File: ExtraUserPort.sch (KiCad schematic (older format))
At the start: 32 parts, among them CN1 EXPANSION_PORT, CN2 ALMOST_USERPORT, CN3 DB9_MALE, J1 ATTENTION_IN, U1 GAL20V8, U2 MOS_6529, U3 MOS_6551_ACIA, U4 74LS652, U5 MAX238, Y1 1.8432M

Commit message: WIP
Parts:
- added RN1: 8.2k, Resistor_THT:R_Array_SIP9, symbol Device:R_Network08
- D1, D2, D3, D4, D5, D6, D7, D8: renamed from D?; value D -> 1n4148; footprint (none) -> Diode_THT:D_DO-35_SOD27_P2.54mm_Vertical_KathodeUp
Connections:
- net +5V: now also RN1.1 (common)
- net p0: now also D1.2 (A), U4.4 (A1); no longer CN2.B (D0), D1.1 (K)
- net p1: now also D2.2 (A), U4.5 (A2); no longer CN2.K (D1), D2.1 (K)
- net p2: now also D3.2 (A), U4.6 (A3); no longer CN2.4 (D2), D3.1 (K)
- net p3: now also D4.2 (A), U4.7 (A4); no longer CN2.5 (D3), D4.1 (K)
- net p4: now also D5.2 (A), U4.8 (A5); no longer CN2.6 (D4), D5.1 (K)
- net p5: now also D6.2 (A), U4.9 (A6); no longer CN2.7 (D5), D6.1 (K)
- net p6: now also D7.2 (A), U4.10 (A7); no longer CN2.J (D6), D7.1 (K)
- net p7: now also D8.2 (A), U4.11 (A8); no longer CN2.F (D7), D8.1 (K)
- new net pc0: CN2.B (D0), D1.1 (K), RN1.2 (R1)
- new net pc1: CN2.K (D1), D2.1 (K), RN1.3 (R2)
- new net pc2: CN2.4 (D2), D3.1 (K), RN1.4 (R3)
- new net pc3: CN2.5 (D3), D4.1 (K), RN1.5 (R4)
- new net pc4: CN2.6 (D4), D5.1 (K), RN1.6 (R5)
- new net pc5: CN2.7 (D5), D6.1 (K), RN1.7 (R6)
- new net pc6: CN2.J (D6), D7.1 (K), RN1.8 (R7)
- new net pc7: CN2.F (D7), D8.1 (K), RN1.9 (R8)
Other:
- note added: "JP1 CONFIGURES MOS 6529/6551 ADDRESSES:\n1-2 = C16 CONFIGURATION: 6529 = $FD1X, 6551 = $FD0X\n (SAME AS PLUS/4 BUILT-IN PORTS)\n2-3 = PLUS/4 CONFIGURATION: 6529 = $FD7X, 6551 = $FD6X\n (FOR ADDITIONAL PORTS)"
- note added: "MOS 6529 REPLACEMENT CIRCUIT\nBY DANIEL MANTIONE"
- note added: "THESE COMPONENTS ARE NEEDED TO MAKE THE 74x652 OUTPUTS\nBEHAVE IN AN OPEN-COLLECTOR FASHION, AS THE ORIGINAL MOS\n6529 OUTPUTS DO.\n\nTHEY MUST BE PLACED THIS WAY (I.E. AFTER THE OUTPUTS EVEN IF\nAN ORIGINAL 6529 IS USED) FOR ROUTING REASONS, THEREFORE IF\n74x654 OR ORIGINAL MOS 6529 IS USED: \n- REPLACE D1-8 WITH 0-OHM RESISTORS \n- DO NOT MOUNT RN1"
- note removed: "$FD60-FD63\n(CONFIGURABLE WITH JP1)"
- note removed: "$FD70"
- note removed: "THESE ADDRESSES ARE THE SAME\nAS SOLDER'S "SPOILER" FOR THE\nSIMILAR PROJECT HE WAS WORKING\nON AND APPARENTLY NEVER COMPLETED"
- moved on the sheet: C1, C3, C5, C6, C7, C8, C9, CN2, CN3, D1, D2, D3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

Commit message: WIP
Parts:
- D1, D2, D3, D4, D5, D6, D7, D8: value 1n4148 -> BAT43
- R1, R2, R3: footprint Resistor_THT:R_Axial_DIN0207_L6.3mm_D2.5mm_P10.16mm_Horizontal -> Resistor_THT:R_Axial_DIN0207_L6.3mm_D2.5mm_P2.54mm_Vertical
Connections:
- net p0: now also D1.1 (K); no longer D1.2 (A)
- net p1: now also D2.1 (K); no longer D2.2 (A)
- net p2: now also D3.1 (K); no longer D3.2 (A)
- net p3: now also D4.1 (K); no longer D4.2 (A)
- net p4: now also D5.1 (K); no longer D5.2 (A)
- net p5: now also D6.1 (K); no longer D6.2 (A)
- net p6: now also D7.1 (K); no longer D7.2 (A)
- net p7: now also D8.1 (K); no longer D8.2 (A)
- net pc0: now also D1.2 (A); no longer D1.1 (K)
- net pc1: now also D2.2 (A); no longer D2.1 (K)
- net pc2: now also D3.2 (A); no longer D3.1 (K)
- net pc3: now also D4.2 (A); no longer D4.1 (K)
- net pc4: now also D5.2 (A); no longer D5.1 (K)
- net pc5: now also D6.2 (A); no longer D6.1 (K)
- net pc6: now also D7.2 (A); no longer D7.1 (K)
- net pc7: now also D8.2 (A); no longer D8.1 (K)
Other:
- note added: "THESE COMPONENTS ARE NEEDED TO MAKE THE 74x652 OUTPUTS\nBEHAVE IN AN OPEN-COLLECTOR FASHION, AS THE ORIGINAL MOS\n6529 OUTPUTS DO.\n\nTHEY MUST BE PLACED THIS WAY (I.E. AFTER THE OUTPUTS EVEN IF\nAN ORIGINAL 6529 IS USED) FOR ROUTING REASONS, THEREFORE IF\n74x654 OR ORIGINAL MOS 6529 IS USED, REPLACE D1-8 WITH\n0-OHM RESISTORS.\n\nIF ORIGINAL MOS 6529 IS USED, DO NOT MOUNT RN1 EITHER."
- note removed: "THESE COMPONENTS ARE NEEDED TO MAKE THE 74x652 OUTPUTS\nBEHAVE IN AN OPEN-COLLECTOR FASHION, AS THE ORIGINAL MOS\n6529 OUTPUTS DO.\n\nTHEY MUST BE PLACED THIS WAY (I.E. AFTER THE OUTPUTS EVEN IF\nAN ORIGINAL 6529 IS USED) FOR ROUTING REASONS, THEREFORE IF\n74x654 OR ORIGINAL MOS 6529 IS USED: \n- REPLACE D1-8 WITH 0-OHM RESISTORS \n- DO NOT MOUNT RN1"
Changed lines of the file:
@@
 F 0 "R2" H 6765 7251 50  0000 L CNN
 F 1 "10k" H 6765 7160 50  0000 L CNN
-F 2 "Resistor_THT:R_Axial_DIN0207_L6.3mm_D2.5mm_P10.16mm_Horizontal" V 6625 7205 50  0001 C CNN
+F 2 "Resistor_THT:R_Axial_DIN0207_L6.3mm_D2.5mm_P2.54mm_Vertical" V 6625 7205 50  0001 C CNN
 F 3 "~" H 6695 7205 50  0001 C CNN
 	1    6695 7205
@@
 F 0 "R1" H 6485 7251 50  0000 L CNN
 F 1 "10k" H 6485 7160 50  0000 L CNN
-F 2 "Resistor_THT:R_Axial_DIN0207_L6.3mm_D2.5mm_P10.16mm_Horizontal" V 6345 7205 50  0001 C CNN
+F 2 "Resistor_THT:R_Axial_DIN0207_L6.3mm_D2.5mm_P2.54mm_Vertical" V 6345 7205 50  0001 C CNN
 F 3 "~" H 6415 7205 50  0001 C CNN
 	1    6415 7205
@@
 F 0 "R3" H 2105 6681 50  0000 R CNN
 F 1 "10k" H 2105 6590 50  0000 R CNN
-F 2 "Resistor_THT:R_Axial_DIN0207_L6.3mm_D2.5mm_P10.16mm_Horizontal" V 2105 6635 50  0001 C CNN
+F 2 "Resistor_THT:R_Axial_DIN0207_L6.3mm_D2.5mm_P2.54mm_Vertical" V 2105 6635 50  0001 C CNN
 F 3 "~" H 2175 6635 50  0001 C CNN
 	1    2175 6635
@@
 P 11140 4640
 F 0 "D2" H 11250 4680 50  0000 C CNN
-F 1 "1n4148" H 11140 4766 50  0001 C CNN
+F 1 "BAT43" H 11140 4766 50  0001 C CNN
 F 2 "Diode_THT:D_DO-35_SOD27_P2.54mm_Vertical_KathodeUp" H 11140 4640 50  0001 C CNN
 F 3 "~" H 11140 4640 50  0001 C CNN
 	1    11140 4640
-	-1   0    0    -1
+	1    0    0    -1
 $EndComp
 Wire Wire Line
@@
 P 11445 4740
 F 0 "D3" H 11560 4780 50  0000 C CNN
-F 1 "1n4148" H 11445 4866 50  0001 C CNN
+F 1 "BAT43" H 11445 4866 50  0001 C CNN
 F 2 "Diode_THT:D_DO-35_SOD27_P2.54mm_Vertical_KathodeUp" H 11445 4740 50  0001 C CNN
 F 3 "~" H 11445 4740 50  0001 C CNN
 	1    11445 4740
-	-1   0    0    -1
+	1    0    0    -1
 $EndComp
 Wire Wire Line
@@
 P 11140 4840
 F 0 "D4" H 11250 4885 50  0000 C CNN
-F 1 "1n4148" H 11140 4966 50  0001 C CNN
+F 1 "BAT43" H 11140 4966 50  0001 C CNN
 F 2 "Diode_THT:D_DO-35_SOD27_P2.54mm_Vertical_KathodeUp" H 11140 4840 50  0001 C CNN
 F 3 "~" H 11140 4840 50  0001 C CNN
 	1    11140 4840
-	-1   0    0    -1
+	1    0    0    -1
 $EndComp
 Wire Wire Line
@@
 P 11140 5040
 F 0 "D6" H 11250 5085 50  0000 C CNN
-F 1 "1n4148" H 11140 5166 50  0001 C CNN
+F 1 "BAT43" H 11140 5166 50  0001 C CNN
 F 2 "Diode_THT:D_DO-35_SOD27_P2.54mm_Vertical_KathodeUp" H 11140 5040 50  0001 C CNN
 F 3 "~" H 11140 5040 50  0001 C CNN
 	1    11140 5040
-	-1   0    0    -1
+	1    0    0    -1
 $EndComp
 Wire Wire Line
@@
 P 11140 5240
 F 0 "D8" H 11250 5280 50  0000 C CNN
-F 1 "1n4148" H 10970 5100 50  0000 C CNN
+F 1 "BAT43" H 11345 5130 50  0000 C CNN
 F 2 "Diode_THT:D_DO-35_SOD27_P2.54mm_Vertical_KathodeUp" H 11140 5240 50  0001 C CNN
 F 3 "~" H 11140 5240 50  0001 C CNN
 	1    11140 5240
-	-1   0    0    -1
+	1    0    0    -1
 $EndComp
 Wire Wire Line
@@
 P 11445 4540
 F 0 "D1" H 11560 4590 50  0000 C CNN
-F 1 "1n4148" H 11585 4800 50  0001 C CNN
+F 1 "BAT43" H 11585 4800 50  0001 C CNN
 F 2 "Diode_THT:D_DO-35_SOD27_P2.54mm_Vertical_KathodeUp" H 11445 4540 50  0001 C CNN
 F 3 "~" H 11445 4540 50  0001 C CNN
 	1    11445 4540
-	-1   0    0    -1
+	1    0    0    -1
 $EndComp
 Wire Wire Line
@@
 P 11445 5140
 F 0 "D7" H 11560 5185 50  0000 C CNN
-F 1 "1n4148" H 11445 5266 50  0001 C CNN
+F 1 "BAT43" H 11445 5266 50  0001 C CNN
 F 2 "Diode_THT:D_DO-35_SOD27_P2.54mm_Vertical_KathodeUp" H 11445 5140 50  0001 C CNN
 F 3 "~" H 11445 5140 50  0001 C CNN
 	1    11445 5140
-	-1   0    0    -1
+	1    0    0    -1
 $EndComp
 Wire Wire Line
@@
 P 11445 4940
 F 0 "D5" H 11560 4980 50  0000 C CNN
-F 1 "1n4148" H 11445 5066 50  0001 C CNN
+F 1 "BAT43" H 11445 5066 50  0001 C CNN
 F 2 "Diode_THT:D_DO-35_SOD27_P2.54mm_Vertical_KathodeUp" H 11445 4940 50  0001 C CNN
 F 3 "~" H 11445 4940 50  0001 C CNN
 	1    11445 4940
-	-1   0    0    -1
+	1    0    0    -1
 $EndComp
 Wire Notes Line
-	11575 4455 11575 5485
+	11640 4420 11640 5450
 Wire Notes Line
-	11575 5485 10970 5485
+	11640 5450 11035 5450
 Wire Notes Line
-	10970 5485 10970 4455
+	11035 5450 11035 4420
 Wire Notes Line
-	10970 4455 11575 4455
-Text Notes 10375 6305 0    50   ~ 0
-THESE COMPONENTS ARE NEEDED TO MAKE THE 74x652 OUTPUTS\nBEHAVE IN AN OPEN-COLLECTOR FASHION, AS THE ORIGINAL MOS\n6529 OUTPUTS DO.\n\nTHEY MUST BE PLACED THIS WAY (I.E. AFTER THE OUTPUTS EVEN IF\nAN ORIGINAL 6529 IS USED) FOR ROUTING REASONS, THEREFORE IF\n74x654 OR ORIGINAL MOS 6529 IS USED: \n- REPLACE D1-8 WITH 0-OHM RESISTORS \n- DO NOT MOUNT RN1
+	11035 4420 11640 4420
+Text Notes 10400 6330 0    50   ~ 0
+THESE COMPONENTS ARE NEEDED TO MAKE THE 74x652 OUTPUTS\nBEHAVE IN AN OPEN-COLLECTOR FASHION, AS THE ORIGINAL MOS\n6529 OUTPUTS DO.\n\nTHEY MUST BE PLACED THIS WAY (I.E. AFTER THE OUTPUTS EVEN IF\nAN ORIGINAL 6529 IS USED) FOR ROUTING REASONS, THEREFORE IF\n74x654 OR ORIGINAL MOS 6529 IS USED, REPLACE D1-8 WITH\n0-OHM RESISTORS.\n\nIF ORIGINAL MOS 6529 IS USED, DO NOT MOUNT RN1 EITHER.
 Text Label 10705 2530 2    50   ~ 0
 p7

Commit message: WIP
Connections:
- net pc0: now also RN1.6 (R5); no longer RN1.2 (R1)
- net pc1: now also RN1.5 (R4); no longer RN1.3 (R2)
- net pc3: now also RN1.3 (R2); no longer RN1.5 (R4)
- net pc4: now also RN1.2 (R1); no longer RN1.6 (R5)
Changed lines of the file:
@@
 	1    0    0    -1
 $EndComp
-Wire Wire Line
-	11290 4640 12265 4640
 $Comp
 L Device:D D3
@@
 	1    0    0    -1
 $EndComp
-Wire Wire Line
-	11595 4740 12165 4740
 $Comp
 L Device:D D4
@@
 	1    0    0    -1
 $EndComp
-Wire Wire Line
-	11290 4840 12065 4840
 $Comp
 L Device:D D6
@@
 $EndComp
 Wire Wire Line
-	12365 4320 12365 4540
-Connection ~ 12365 4540
-Wire Wire Line
-	12365 4540 12725 4540
-Wire Wire Line
-	12265 4320 12265 4640
-Connection ~ 12265 4640
-Wire Wire Line
-	12265 4640 12725 4640
-Wire Wire Line
-	12165 4320 12165 4740
-Connection ~ 12165 4740
-Wire Wire Line
-	12165 4740 12725 4740
-Wire Wire Line
-	12065 4320 12065 4840
-Connection ~ 12065 4840
-Wire Wire Line
-	12065 4840 12725 4840
-Wire Wire Line
-	11965 4320 11965 4940
-Connection ~ 11965 4940
-Wire Wire Line
-	11965 4940 12725 4940
-Wire Wire Line
 	11865 4320 11865 5040
 Connection ~ 11865 5040
@@
 Text Notes 8430 3735 0    50   ~ 0
 MOS 6529 REPLACEMENT CIRCUIT\nBY DANIEL MANTIONE
-Wire Wire Line
-	11595 4540 12365 4540
 $Comp
 L Device:D D1
@@
 	1    0    0    -1
 $EndComp
-Wire Wire Line
-	11595 4940 11965 4940
 $Comp
 L Device:D D5
@@
 Wire Wire Line
 	10715 5140 11295 5140
+Wire Wire Line
+	11595 4540 11965 4540
+Wire Wire Line
+	11290 4640 12065 4640
+Wire Wire Line
+	11595 4740 12165 4740
+Wire Wire Line
+	11290 4840 12265 4840
+Wire Wire Line
+	11595 4940 12365 4940
+Wire Wire Line
+	12365 4320 12365 4940
+Connection ~ 12365 4940
+Wire Wire Line
+	12365 4940 12725 4940
+Wire Wire Line
+	12265 4320 12265 4840
+Connection ~ 12265 4840
+Wire Wire Line
+	12265 4840 12725 4840
+Wire Wire Line
+	12165 4320 12165 4740
+Connection ~ 12165 4740
+Wire Wire Line
+	12165 4740 12725 4740
+Wire Wire Line
+	12065 4320 12065 4640
+Connection ~ 12065 4640
+Wire Wire Line
+	12065 4640 12725 4640
+Wire Wire Line
+	11965 4320 11965 4540
 Wire Bus Line
 	15640 1415 15640 2945
@@
 Wire Bus Line
 	5450 1450 5450 2555
+Connection ~ 11965 4540
+Wire Wire Line
+	11965 4540 12725 4540
 $EndSCHEMATC

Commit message: WIP
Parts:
- added J2: TAPE_IN, ExtraUserPort:Connector_Mini-DIN_Female_8Pin_2rows, symbol mini-din-8:Mini-DIN-8
- added JP4: JMP_CASS_SENSE, Jumper:SolderJumper-2_P1.3mm_Bridged_RoundedPad1.0x1.5mm, symbol Device:Jumper_NC_Small
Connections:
- net GND: now also J2.0 (SH), J2.8
- net pc2: now also JP4.2
- net cst_motor: no longer names the net of U1.17 (IO17)
- net cst_sense_in: no longer names the net of U1.18 (IO18)
- net cst_sense_out: no longer names the net of U1.20 (I020)
- new net ~cassette_sense: J2.7, JP4.1
- no-connect marks 20 -> 29
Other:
- note added: "CASSETTE SENSE"
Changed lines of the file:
@@
 Sheet 1 1
 Title "ExtraUserPort"
-Date "2022-09-10"
+Date "2022-09-12"
 Rev "1git"
 Comp "SukkoPera & The Folks From The Plus/4 World Forum"
@@
 	7050 1655 7550 1655
 Wire Wire Line
-	7050 1755 7550 1755
-Wire Wire Line
 	7050 1855 7550 1855
-Wire Wire Line
-	7050 1955 7550 1955
-Wire Wire Line
-	7050 2055 7550 2055
 Text Label 7550 1555 2    50   ~ 0
 gab
@@
 Text Label 7550 1855 2    50   ~ 0
 r_~w
-Text Label 7550 2055 2    50   ~ 0
-cst_motor
-Text Label 7550 1955 2    50   ~ 0
-cst_sense_in
-Text Label 7550 1755 2    50   ~ 0
-cst_sense_out
 $Comp
 L Connector:Conn_01x03_Male JP1
@@
 Wire Wire Line
 	11965 4320 11965 4540
+Connection ~ 11965 4540
+Wire Wire Line
+	11965 4540 12725 4540
+$Comp
+L mini-din-8:Mini-DIN-8 J2
+U 1 1 63742584
+P 5790 10060
+F 0 "J2" H 6040 9780 50  0000 C CNN
+F 1 "TAPE_IN" H 6040 9685 50  0000 C CNN
+F 2 "ExtraUserPort:Connector_Mini-DIN_Female_8Pin_2rows" V 5780 10050 50  0001 C CNN
+F 3 "http://service.powerdynamics.com/ec/Catalog17/Section%2011.pdf" V 5780 10050 50  0001 C CNN
+	1    5790 10060
+	1    0    0    -1
+$EndComp
+Wire Wire Line
+	5490 9960 5350 9960
+Wire Wire Line
+	5350 9960 5350 10485
+$Comp
+L power:GND #PWR04
+U 1 1 6376DC4F
+P 5790 10580
+F 0 "#PWR04" H 5790 10330 50  0001 C CNN
+F 1 "GND" H 5795 10407 50  0000 C CNN
+F 2 "" H 5790 10580 50  0001 C CNN
+F 3 "" H 5790 10580 50  0001 C CNN
+	1    5790 10580
+	1    0    0    -1
+$EndComp
+Wire Wire Line
+	5790 10360 5790 10485
+Wire Wire Line
+	5790 10485 5350 10485
+Wire Wire Line
+	5790 10485 5790 10580
+Connection ~ 5790 10485
+NoConn ~ 6090 10260
+NoConn ~ 6090 10160
+NoConn ~ 6090 10060
+NoConn ~ 6090 9960
+NoConn ~ 5490 10060
+NoConn ~ 5490 10160
+Wire Wire Line
+	5790 9760 5790 9675
+Wire Wire Line
+	5790 9675 6465 9675
+NoConn ~ 7050 1755
+NoConn ~ 7050 1955
+NoConn ~ 7050 2055
+Text Label 6420 9675 2    50   ~ 0
+~cassette_sense
+$Comp
+L Device:Jumper_NC_Small JP4
+U 1 1 6398A408
+P 6565 9675
+F 0 "JP4" H 6565 9887 50  0000 C CNN
+F 1 "JMP_CASS_SENSE" H 6565 9796 50  0000 C CNN
+F 2 "Jumper:SolderJumper-2_P1.3mm_Bridged_RoundedPad1.0x1.5mm" H 6565 9675 50  0001 C CNN
+F 3 "~" H 6565 9675 50  0001 C CNN
+	1    6565 9675
+	1    0    0    -1
+$EndComp
+Entry Wire Line
+	7030 9775 6930 9675
+Wire Bus Line
+	7030 9775 7665 9775
+Text Label 7665 9775 2    50   ~ 0
+oc_parallel_port
+Text Label 6930 9675 2    50   ~ 0
+pc2
+Wire Wire Line
+	6665 9675 6930 9675
+Wire Bus Line
+	7030 9770 7030 9775
+Text Notes 6290 9345 0    50   ~ 0
+CASSETTE SENSE
 Wire Bus Line
 	15640 1415 15640 2945
@@
 Wire Bus Line
 	5450 1450 5450 2555
-Connection ~ 11965 4540
-Wire Wire Line
-	11965 4540 12725 4540
 $EndSCHEMATC

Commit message: WIP
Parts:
- renumbered U4 to U102, U5 to U4
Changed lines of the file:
@@
 	9995 7500 9995 7905
 $Comp
-L MAX238:MAX238 U5
+L MAX238:MAX238 U4
 U 1 1 6473EB86
 P 11195 8155
-F 0 "U5" H 11195 9070 50  0000 C CNN
+F 0 "U4" H 11195 9070 50  0000 C CNN
 F 1 "MAX238" H 11195 8979 50  0000 C CNN
 F 2 "Package_DIP:DIP-24_W7.62mm_Socket_LongPads" H 11195 8155 50  0001 C CNN
@@
 OR GAL22V16
 $Comp
-L 74LS652:74LS652 U4
+L 74LS652:74LS652 U102
 U 1 1 63CCDE81
 P 8175 4795
-F 0 "U4" H 8175 5710 50  0000 C CNN
+F 0 "U102" H 8175 5710 50  0000 C CNN
 F 1 "74LS652" H 8175 5619 50  0000 C CNN
 F 2 "Package_DIP:DIP-24_W7.62mm_Socket_LongPads" H 8175 4795 50  0001 C CNN

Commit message: wip
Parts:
- renumbered C5 to C4, C9 to C5
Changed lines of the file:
@@
 	12540 8505 12540 8670
 $Comp
-L Device:CP1 C9
+L Device:CP1 C5
 U 1 1 647877C0
 P 12540 8820
-F 0 "C9" H 12425 8774 50  0000 R CNN
+F 0 "C5" H 12425 8774 50  0000 R CNN
 F 1 "1u" H 12425 8865 50  0000 R CNN
 F 2 "Capacitor_THT:CP_Radial_D5.0mm_P2.00mm" H 12540 8820 50  0001 C CNN
@@
 $EndComp
 $Comp
-L Device:CP1 C5
+L Device:CP1 C4
 U 1 1 647D3BC2
 P 11185 9480
-F 0 "C5" H 11300 9526 50  0000 L CNN
+F 0 "C4" H 11300 9526 50  0000 L CNN
 F 1 "1u" H 11300 9435 50  0000 L CNN
 F 2 "Capacitor_THT:CP_Radial_D5.0mm_P2.00mm" H 11185 9480 50  0001 C CNN

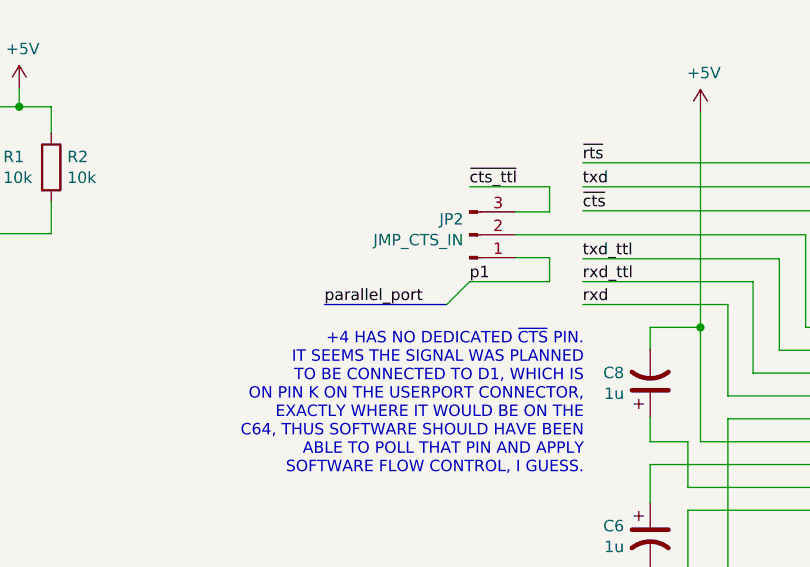
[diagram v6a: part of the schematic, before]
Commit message: Move /CTS to PC2
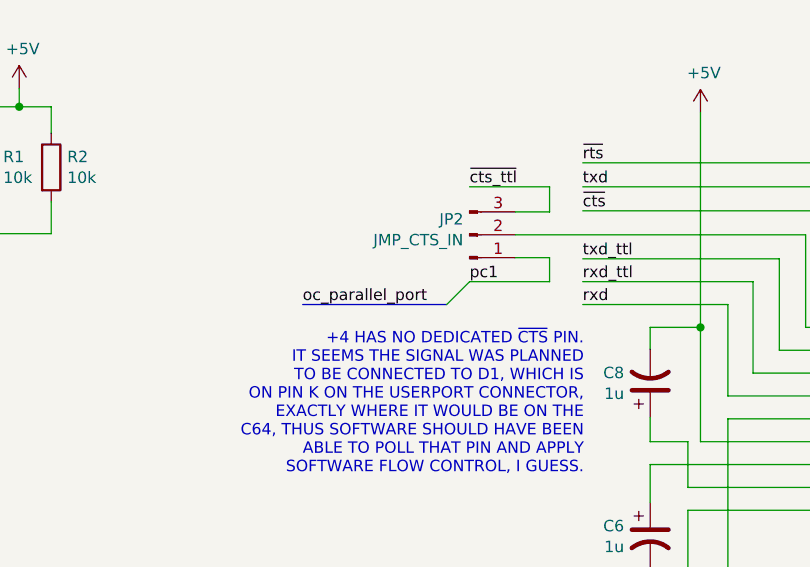
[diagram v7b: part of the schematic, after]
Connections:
- net p1: no longer JP2.1 (Pin_1)
- net pc1: now also JP2.1 (Pin_1)
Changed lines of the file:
@@
 	8525 7705 8425 7805
 Text Label 8525 7705 0    50   ~ 0
-p1
+pc1
 Wire Bus Line
-	8425 7805 7890 7805
-Text Label 7890 7805 0    50   ~ 0
-parallel_port
+	8425 7805 7795 7805
+Text Label 7795 7805 0    50   ~ 0
+oc_parallel_port
 Text Notes 9025 8550 2    50   ~ 0
 +4 HAS NO DEDICATED ~CTS~ PIN.\nIT SEEMS THE SIGNAL WAS PLANNED\nTO BE CONNECTED TO D1, WHICH IS\nON PIN K ON THE USERPORT CONNECTOR,\nEXACTLY WHERE IT WOULD BE ON THE\nC64, THUS SOFTWARE SHOULD HAVE BEEN\nABLE TO POLL THAT PIN AND APPLY\nSOFTWARE FLOW CONTROL, I GUESS.

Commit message: Almost ready for prototypes
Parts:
- removed JP4: JMP_CASS_SENSE, Jumper:SolderJumper-2_P1.3mm_Bridged_RoundedPad1.0x1.5mm, symbol Device:Jumper_NC_Small
- added R4, R5: 1k, Resistor_THT:R_Axial_DIN0207_L6.3mm_D2.5mm_P2.54mm_Vertical, symbol Device:R
- added V0: LOGO, ExtraUserPort:logo, symbol void:Void
- added V1: CC-BY-NC-SA, ExtraUserPort:cc_by_nc_sa, symbol void:Void
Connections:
- net pc1: now also R5.2; no longer JP2.1 (Pin_1)
- net pc2: now also R4.1
- net ~cassette_sense: now also R4.2
- new net: JP2.1 (Pin_1), R5.1
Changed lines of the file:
@@
 Sheet 1 1
 Title "ExtraUserPort"
-Date "2022-09-12"
+Date "2022-09-17"
 Rev "1git"
 Comp "SukkoPera & The Folks From The Plus/4 World Forum"
@@
 	8875 7600 8875 7705
 Wire Wire Line
-	8875 7705 8525 7705
-Entry Wire Line
-	8525 7705 8425 7805
-Text Label 8525 7705 0    50   ~ 0
+	8875 7705 8770 7705
+Entry Wire Line
+	8285 7705 8185 7805
+Text Label 8285 7705 0    50   ~ 0
 pc1
 Wire Bus Line
-	8425 7805 7795 7805
-Text Label 7795 7805 0    50   ~ 0
+	8185 7805 7555 7805
+Text Label 7555 7805 0    50   ~ 0
 oc_parallel_port
-Text Notes 9025 8550 2    50   ~ 0
+Text Notes 8955 8690 2    50   ~ 0
 +4 HAS NO DEDICATED ~CTS~ PIN.\nIT SEEMS THE SIGNAL WAS PLANNED\nTO BE CONNECTED TO D1, WHICH IS\nON PIN K ON THE USERPORT CONNECTOR,\nEXACTLY WHERE IT WOULD BE ON THE\nC64, THUS SOFTWARE SHOULD HAVE BEEN\nABLE TO POLL THAT PIN AND APPLY\nSOFTWARE FLOW CONTROL, I GUESS.
 Wire Wire Line
@@
 Wire Wire Line
 	5790 9760 5790 9675
-Wire Wire Line
-	5790 9675 6465 9675
 NoConn ~ 7050 1755
 NoConn ~ 7050 1955
@@
 Text Label 6420 9675 2    50   ~ 0
 ~cassette_sense
-$Comp
-L Device:Jumper_NC_Small JP4
-U 1 1 6398A408
-P 6565 9675
-F 0 "JP4" H 6565 9887 50  0000 C CNN
-F 1 "JMP_CASS_SENSE" H 6565 9796 50  0000 C CNN
-F 2 "Jumper:SolderJumper-2_P1.3mm_Bridged_RoundedPad1.0x1.5mm" H 6565 9675 50  0001 C CNN
-F 3 "~" H 6565 9675 50  0001 C CNN
-	1    6565 9675
-	1    0    0    -1
-$EndComp
-Entry Wire Line
-	7030 9775 6930 9675
+Entry Wire Line
+	7140 9775 7040 9675
 Wire Bus Line
-	7030 9775 7665 9775
-Text Label 7665 9775 2    50   ~ 0
+	7140 9775 7775 9775
+Text Label 7775 9775 2    50   ~ 0
 oc_parallel_port
-Text Label 6930 9675 2    50   ~ 0
+Text Label 7040 9675 2    50   ~ 0
 pc2
-Wire Wire Line
-	6665 9675 6930 9675
 Wire Bus Line
-	7030 9770 7030 9775
+	7140 9770 7140 9775
 Text Notes 6290 9345 0    50   ~ 0
 CASSETTE SENSE
+$Comp
+L Device:R R5
+U 1 1 641850A0
+P 8620 7705
+F 0 "R5" V 8735 7705 50  0000 C CNN
+F 1 "1k" V 8826 7705 50  0000 C CNN
+F 2 "Resistor_THT:R_Axial_DIN0207_L6.3mm_D2.5mm_P2.54mm_Vertical" V 8550 7705 50  0001 C CNN
+F 3 "~" H 8620 7705 50  0001 C CNN
+	1    8620 7705
+	0    1    1    0
+$EndComp
+Wire Wire Line
+	8470 7705 8285 7705
+$Comp
+L Device:R R4
+U 1 1 641AD24B
+P 6715 9675
+F 0 "R4" V 6830 9675 50  0000 C CNN
+F 1 "1k" V 6921 9675 50  0000 C CNN
+F 2 "Resistor_THT:R_Axial_DIN0207_L6.3mm_D2.5mm_P2.54mm_Vertical" V 6645 9675 50  0001 C CNN
+F 3 "~" H 6715 9675 50  0001 C CNN
+	1    6715 9675
+	0    1    1    0
+$EndComp
+Wire Wire Line
+	6865 9675 7040 9675
+$Comp
+L void:Void V0
+U 1 1 64272105
+P 11000 11025
+F 0 "V0" H 11078 11071 50  0000 L CNN
+F 1 "LOGO" H 11078 10980 50  0000 L CNN
+F 2 "ExtraUserPort:logo" H 11000 11025 50  0001 C CNN
+F 3 "" H 11000 11025 50  0001 C CNN
+	1    11000 11025
+	1    0    0    -1
+$EndComp
+$Comp
+L void:Void V1
+U 1 1 64272908
+P 11000 10800
+F 0 "V1" H 11078 10846 50  0000 L CNN
+F 1 "CC-BY-NC-SA" H 11078 10755 50  0000 L CNN
+F 2 "ExtraUserPort:cc_by_nc_sa" H 11000 10800 50  0001 C CNN
+F 3 "" H 11000 10800 50  0001 C CNN
+	1    11000 10800
+	1    0    0    -1
+$EndComp
+Wire Wire Line
+	5790 9675 6565 9675
 Wire Bus Line
 	15640 1415 15640 2945
